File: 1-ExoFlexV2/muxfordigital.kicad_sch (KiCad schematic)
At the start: 17 parts, among them U100 SN74LVC3G14DCUT_V2, U101 SN74LVC3G14DCUT_V2, U102 SN74LVC1G08DBVR, U103 SN74LVC3G14DCUT_V2, U104 SN74LVC3G14DCUT_V2, U105 SN74LVC3G14DCUT_V2, U106 SN74LVC3G14DCUT_V2, U107 SN74LVC1G32DBVR, U112 SN74LVC1G32DBVR, U113 SN74LVC1G32DBVR, U97 SN74LVC1G08DBVR, U98 SN74LVC1G08DBVR, U99 SN74LVC1G08DBVR

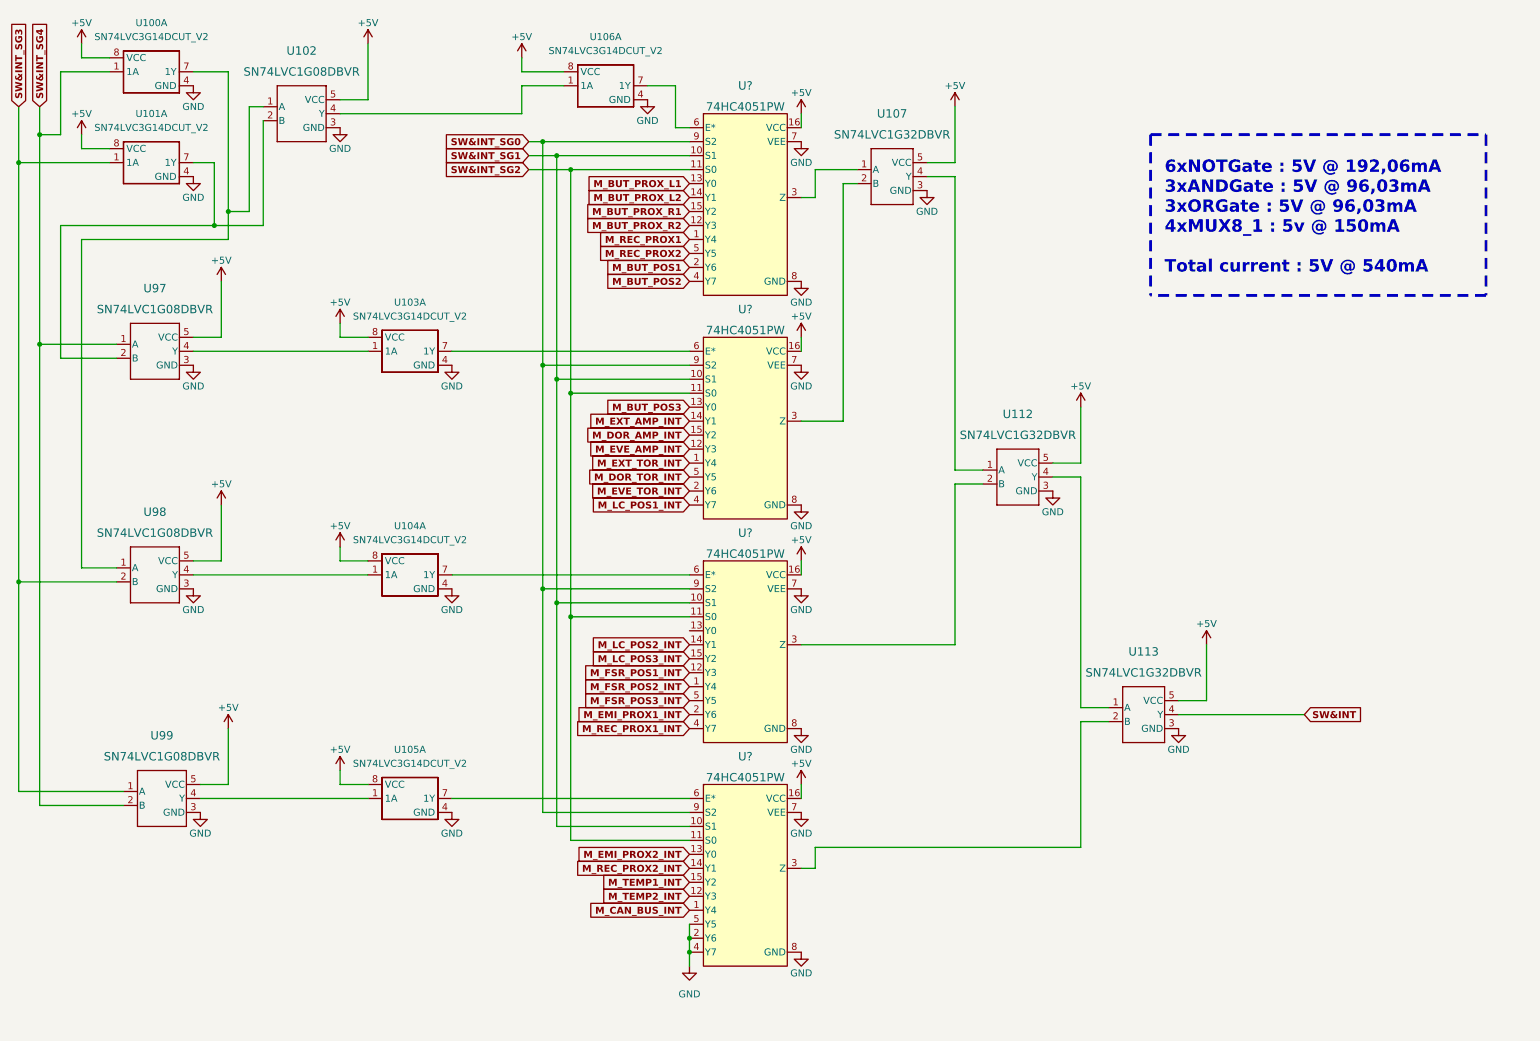
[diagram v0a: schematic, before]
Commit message: Chokes et RC
- Ajout des RF chokes
- Changement des résistance pour 0805
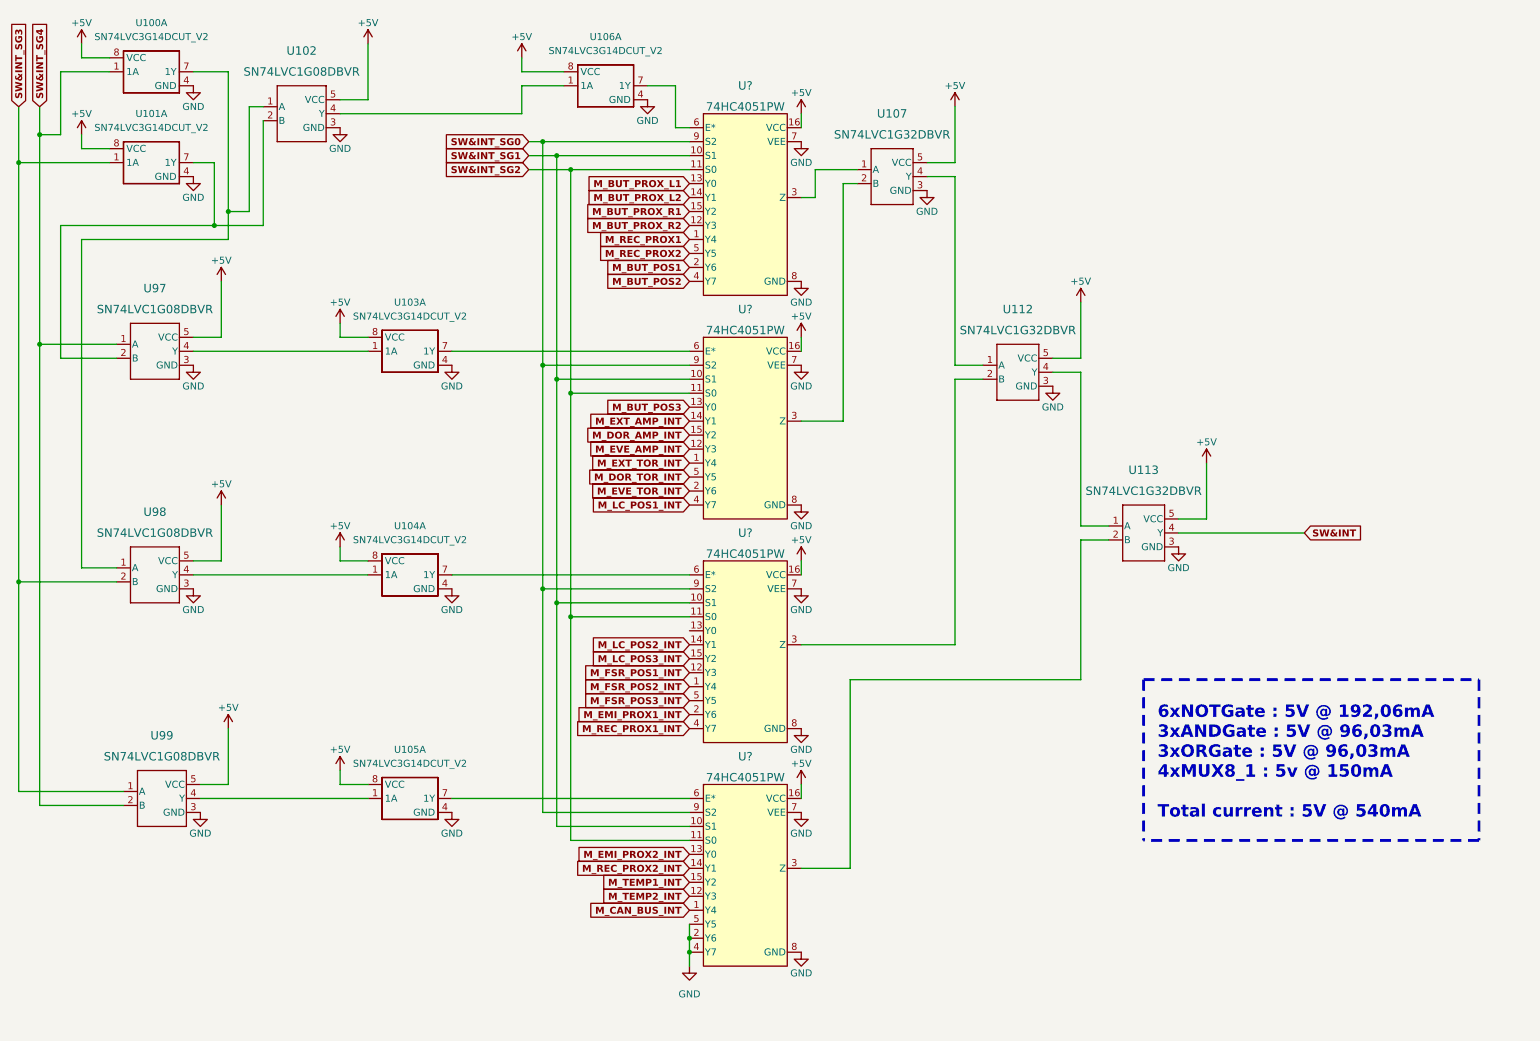
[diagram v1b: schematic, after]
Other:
- moved on the sheet: U112, U113

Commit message: Test points et notes
- Ajout de tous les tests point nécessaires
-  Ajoute des sections de notes dans chaque page
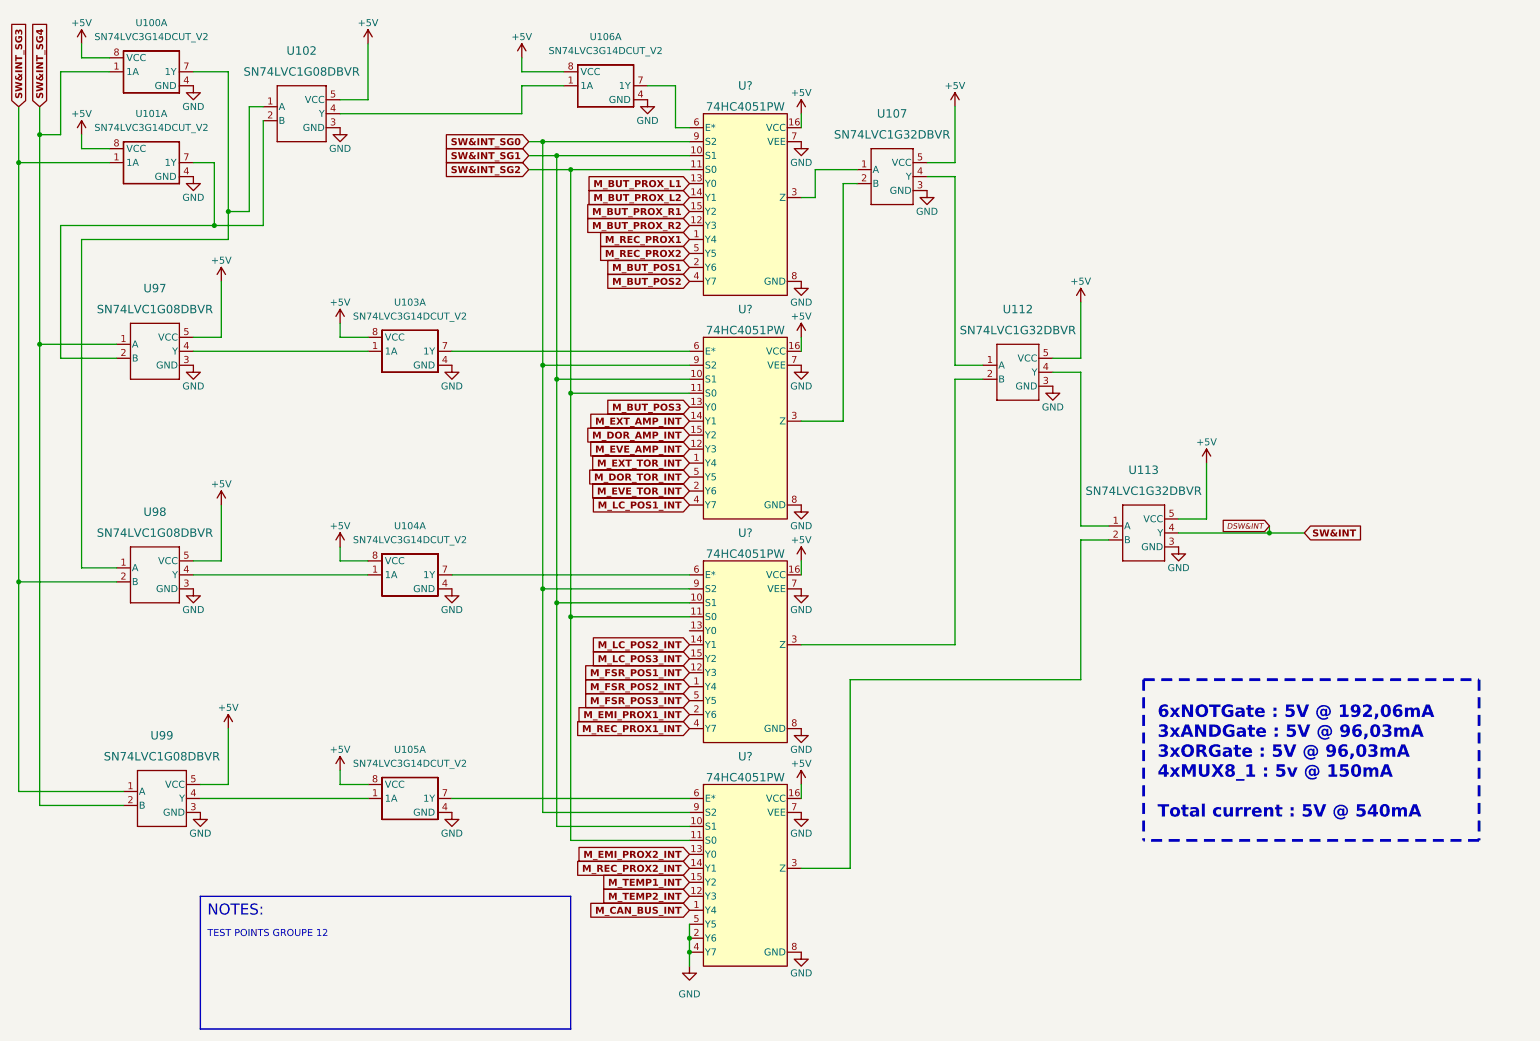
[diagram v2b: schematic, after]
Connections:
- net SW&INT renamed DSW&INT
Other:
- note added: "NOTES:"
- note added: "TEST POINTS GROUPE 12"
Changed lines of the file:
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@@
   (junction (at 115.57 81.28) (diameter 0) (color 0 0 0 0)
   )
+  (junction (at 242.57 106.68) (diameter 0) (color 0 0 0 0)
+  )
   (junction (at 110.49 35.56) (diameter 0) (color 0 0 0 0)
   )
@@
     (stroke (width 0) (type default) (color 0 0 0 0))
   )
+  (polyline (pts (xy 48.26 172.72) (xy 48.26 196.85))
+    (stroke (width 0.25) (type solid) (color 0 0 0 0))
+  )
   (wire (pts (xy 73.66 30.48) (xy 106.68 30.48))
     (stroke (width 0) (type default) (color 0 0 0 0))
@@
   )
   (wire (pts (xy 180.34 41.91) (xy 185.42 41.91))
+    (stroke (width 0) (type default) (color 0 0 0 0))
+  )
+  (wire (pts (xy 242.57 105.41) (xy 242.57 106.68))
     (stroke (width 0) (type default) (color 0 0 0 0))
   )
@@
     (stroke (width 0) (type default) (color 0 0 0 0))
   )
-  (wire (pts (xy 226.06 106.68) (xy 248.92 106.68))
+  (wire (pts (xy 226.06 106.68) (xy 242.57 106.68))
     (stroke (width 0) (type default) (color 0 0 0 0))
   )
@@
   (wire (pts (xy 157.48 111.76) (xy 157.48 114.3))
     (stroke (width 0) (type default) (color 0 0 0 0))
+  )
+  (polyline (pts (xy 115.57 172.72) (xy 115.57 196.85))
+    (stroke (width 0.25) (type solid) (color 0 0 0 0))
   )
   (wire (pts (xy 137.16 177.8) (xy 137.16 180.34))
@@
     (stroke (width 0) (type default) (color 0 0 0 0))
   )
+  (wire (pts (xy 242.57 106.68) (xy 248.92 106.68))
+    (stroke (width 0) (type default) (color 0 0 0 0))
+  )
   (wire (pts (xy 19.05 29.21) (xy 19.05 34.29))
     (stroke (width 0) (type default) (color 0 0 0 0))
@@
     (stroke (width 0) (type default) (color 0 0 0 0))
   )
+  (polyline (pts (xy 48.26 172.72) (xy 115.57 172.72))
+    (stroke (width 0.25) (type solid) (color 0 0 0 0))
+  )
   (wire (pts (xy 115.57 121.92) (xy 115.57 162.56))
     (stroke (width 0) (type default) (color 0 0 0 0))
@@
     (stroke (width 0) (type default) (color 0 0 0 0))
   )
+  (polyline (pts (xy 115.57 196.85) (xy 48.26 196.85))
+    (stroke (width 0.25) (type solid) (color 0 0 0 0))
+  )
   (wire (pts (xy 180.34 39.37) (xy 185.42 39.37))
     (stroke (width 0) (type default) (color 0 0 0 0))
+  )
+  (text "TEST POINTS GROUPE 12" (at 49.53 180.34 0)
+    (effects (font (size 1.27 1.27)) (justify left bottom))
   )
   (text "6xNOTGate : 5V @ 192,06mA\n3xANDGate : 5V @ 96,03mA\n3xORGate : 5V @ 96,03mA\n4xMUX8_1 : 5v @ 150mA\n\nTotal current : 5V @ 540mA"
@@
     (effects (font (size 2.25 2.25) (thickness 0.5) bold) (justify left bottom))
   )
+  (text "NOTES:" (at 49.53 176.53 0)
+    (effects (font (size 2 2)) (justify left bottom))
+  )
+  (global_label "DSW&INT" (shape input) (at 242.57 105.41 180) (fields_autoplaced)
+    (effects (font (size 1 1) italic) (justify right))
+    (property "Intersheet References" "${INTERSHEET_REFS}" (id 0) (at 233.6997 105.3475 0)
+      (effects (font (size 1 1) italic) (justify right) hide)
+    )
+  )
   (global_label "M_LC_POS1_INT" (shape input) (at 137.16 101.6 180) (fields_autoplaced)

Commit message: Schématisation terminée
- Schéma terminé
- Passage vers le PCB
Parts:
- U104: renamed from U97; value SN74LVC1G08DBVR -> AND Gate; DESCRIPTION (none) -> AND Gate IC 1 Channel SOT-23-5; MANUFACTURER (none) -> Texas Instruments; PACKAGE (none) -> SC-74A, SOT-753; PART NUMBER (none) -> SN74LVC1G08DBVR; TYPE (none) -> SMD
- U105: renamed from U98; value SN74LVC1G08DBVR -> AND Gate; DESCRIPTION (none) -> AND Gate IC 1 Channel SOT-23-5; MANUFACTURER (none) -> Texas Instruments; PACKAGE (none) -> SC-74A, SOT-753; PART NUMBER (none) -> SN74LVC1G08DBVR; TYPE (none) -> SMD
- U106: renamed from U99; value SN74LVC1G08DBVR -> AND Gate; DESCRIPTION (none) -> AND Gate IC 1 Channel SOT-23-5; MANUFACTURER (none) -> Texas Instruments; PACKAGE (none) -> SC-74A, SOT-753; PART NUMBER (none) -> SN74LVC1G08DBVR; TYPE (none) -> SMD
- U107: renamed from U100; value SN74LVC3G14DCUT_V2 -> Inverter; DESCRIPTION (none) -> Inverter IC 3 Channel Schmitt Trigger 8-VSSOP; MANUFACTURER (none) -> Texas Instruments; PACKAGE (none) -> 8-VFSOP (0.091", 2.30mm Width); PART NUMBER (none) -> SN74LVC3G14DCUT; TYPE (none) -> SMD
- U108: renamed from U101; value SN74LVC3G14DCUT_V2 -> Inverter; DESCRIPTION (none) -> Inverter IC 3 Channel Schmitt Trigger 8-VSSOP; MANUFACTURER (none) -> Texas Instruments; PACKAGE (none) -> 8-VFSOP (0.091", 2.30mm Width); PART NUMBER (none) -> SN74LVC3G14DCUT; TYPE (none) -> SMD
- U109: renamed from U102; value SN74LVC1G08DBVR -> AND Gate; DESCRIPTION (none) -> AND Gate IC 1 Channel SOT-23-5; MANUFACTURER (none) -> Texas Instruments; PACKAGE (none) -> SC-74A, SOT-753; PART NUMBER (none) -> SN74LVC1G08DBVR; TYPE (none) -> SMD
- U110: renamed from U103; value SN74LVC3G14DCUT_V2 -> Inverter; DESCRIPTION (none) -> Inverter IC 3 Channel Schmitt Trigger 8-VSSOP; MANUFACTURER (none) -> Texas Instruments; PACKAGE (none) -> 8-VFSOP (0.091", 2.30mm Width); PART NUMBER (none) -> SN74LVC3G14DCUT; TYPE (none) -> SMD
- U111: renamed from U104; value SN74LVC3G14DCUT_V2 -> Inverter; DESCRIPTION (none) -> Inverter IC 3 Channel Schmitt Trigger 8-VSSOP; MANUFACTURER (none) -> Texas Instruments; PACKAGE (none) -> 8-VFSOP (0.091", 2.30mm Width); PART NUMBER (none) -> SN74LVC3G14DCUT; TYPE (none) -> SMD
- U112: renamed from U105; value SN74LVC3G14DCUT_V2 -> Inverter; DESCRIPTION (none) -> Inverter IC 3 Channel Schmitt Trigger 8-VSSOP; MANUFACTURER (none) -> Texas Instruments; PACKAGE (none) -> 8-VFSOP (0.091", 2.30mm Width); PART NUMBER (none) -> SN74LVC3G14DCUT; TYPE (none) -> SMD
- U113: renamed from U106; value SN74LVC3G14DCUT_V2 -> Inverter; DESCRIPTION (none) -> Inverter IC 3 Channel Schmitt Trigger 8-VSSOP; MANUFACTURER (none) -> Texas Instruments; PACKAGE (none) -> 8-VFSOP (0.091", 2.30mm Width); PART NUMBER (none) -> SN74LVC3G14DCUT; TYPE (none) -> SMD
- U114, U115, U116, U117: renamed from U?; value 74HC4051PW -> MUX 8:1; DESCRIPTION (none) -> 1 Circuit IC Switch 8:1 120Ohm 16-TSSOP; MANUFACTURER (none) -> Nexperia USA Inc.; PACKAGE (none) -> 16-TSSOP (0.173", 4.40mm Width); PART NUMBER (none) -> 74HC4051PW,118; TYPE (none) -> SMD
- U118: renamed from U107; value SN74LVC1G32DBVR -> OR Gate; DESCRIPTION (none) -> OR Gate IC 1 Channel SOT-23-5; MANUFACTURER (none) -> Texas Instruments; PACKAGE (none) -> SC-74A, SOT-753; PART NUMBER (none) -> SN74LVC1G32DBVR; TYPE (none) -> SMD
- U119: renamed from U112; value SN74LVC1G32DBVR -> OR Gate; DESCRIPTION (none) -> OR Gate IC 1 Channel SOT-23-5; MANUFACTURER (none) -> Texas Instruments; PACKAGE (none) -> SC-74A, SOT-753; PART NUMBER (none) -> SN74LVC1G32DBVR; TYPE (none) -> SMD
- U120: renamed from U113; value SN74LVC1G32DBVR -> OR Gate; DESCRIPTION (none) -> OR Gate IC 1 Channel SOT-23-5; MANUFACTURER (none) -> Texas Instruments; PACKAGE (none) -> SC-74A, SOT-753; PART NUMBER (none) -> SN74LVC1G32DBVR; TYPE (none) -> SMD
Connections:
- net GND: now also U116.4 (Y7)
- net M_EMI_PROX1_INT: now also U116.5 (Y5); no longer U116.2 (Y6)
- net M_FSR_POS1_INT: now also U116.15 (Y2); no longer U116.12 (Y3)
- net M_FSR_POS2_INT: now also U116.12 (Y3); no longer U116.1 (Y4)
- net M_FSR_POS3_INT: now also U116.1 (Y4); no longer U116.5 (Y5)
- net M_LC_POS2_INT: now also U116.13 (Y0); no longer U116.14 (Y1)
- net M_LC_POS3_INT: now also U116.14 (Y1); no longer U116.15 (Y2)
- net M_REC_PROX1_INT: now also U116.2 (Y6); no longer U116.4 (Y7)
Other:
- note added: "6xNOTGate : 5V @ 192,06mA 3xANDGate : 5V @ 96,03mA 3xORGate : 5V @ 96,03mA 4xMUX8_1 : 5v @ 150mA Total current : 5V @ 539mA"
- note removed: "6xNOTGate : 5V @ 192,06mA 3xANDGate : 5V @ 96,03mA 3xORGate : 5V @ 96,03mA 4xMUX8_1 : 5v @ 150mA Total current : 5V @ 540mA"

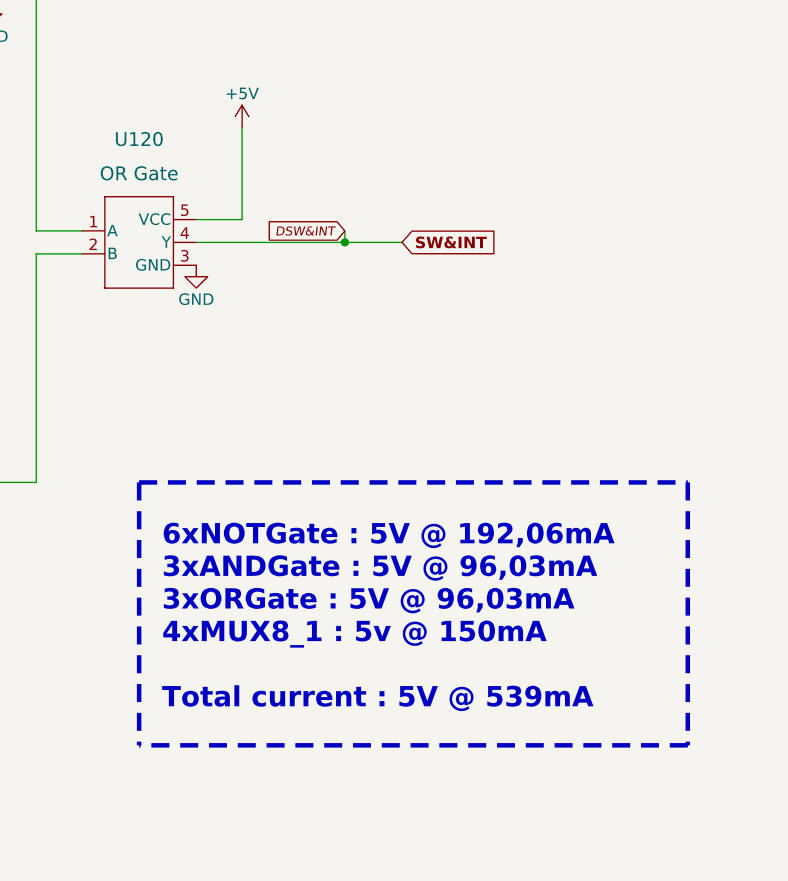
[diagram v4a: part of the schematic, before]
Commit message: Finalisation 3
- Changement des régulateur de tension
- Retrait de test point inutile
- Changement de jumper mal positionner
- Ajout de Mounting holes et fiducial
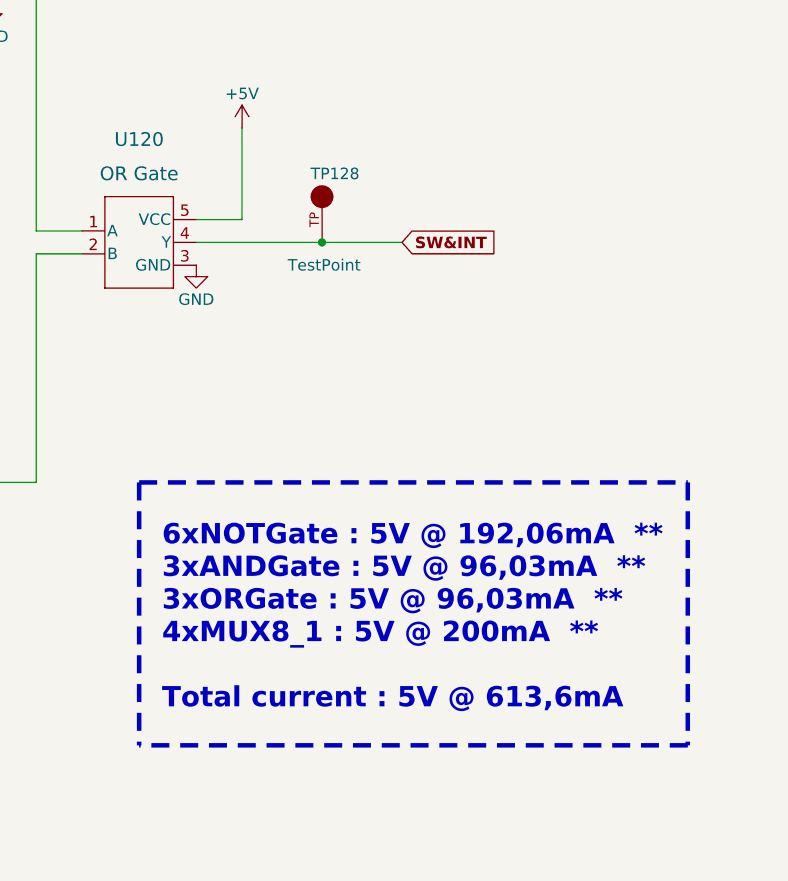
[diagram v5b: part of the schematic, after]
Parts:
- added TP128: TestPoint, FootPrint:KEYSTONE_5005, symbol SymLib:5005
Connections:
- net DSW&INT renamed SW&INT
- net SW&INT: now also TP128.TP
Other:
- note added: "6xNOTGate : 5V @ 192,06mA ** 3xANDGate : 5V @ 96,03mA ** 3xORGate : 5V @ 96,03mA ** 4xMUX8_1 : 5V @ 200mA ** Total current : 5V @ 613,6mA"
- note removed: "6xNOTGate : 5V @ 192,06mA 3xANDGate : 5V @ 96,03mA 3xORGate : 5V @ 96,03mA 4xMUX8_1 : 5v @ 150mA Total current : 5V @ 539mA"
